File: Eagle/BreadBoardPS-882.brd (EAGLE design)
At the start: 36.5 x 16.5 mm, 6 parts

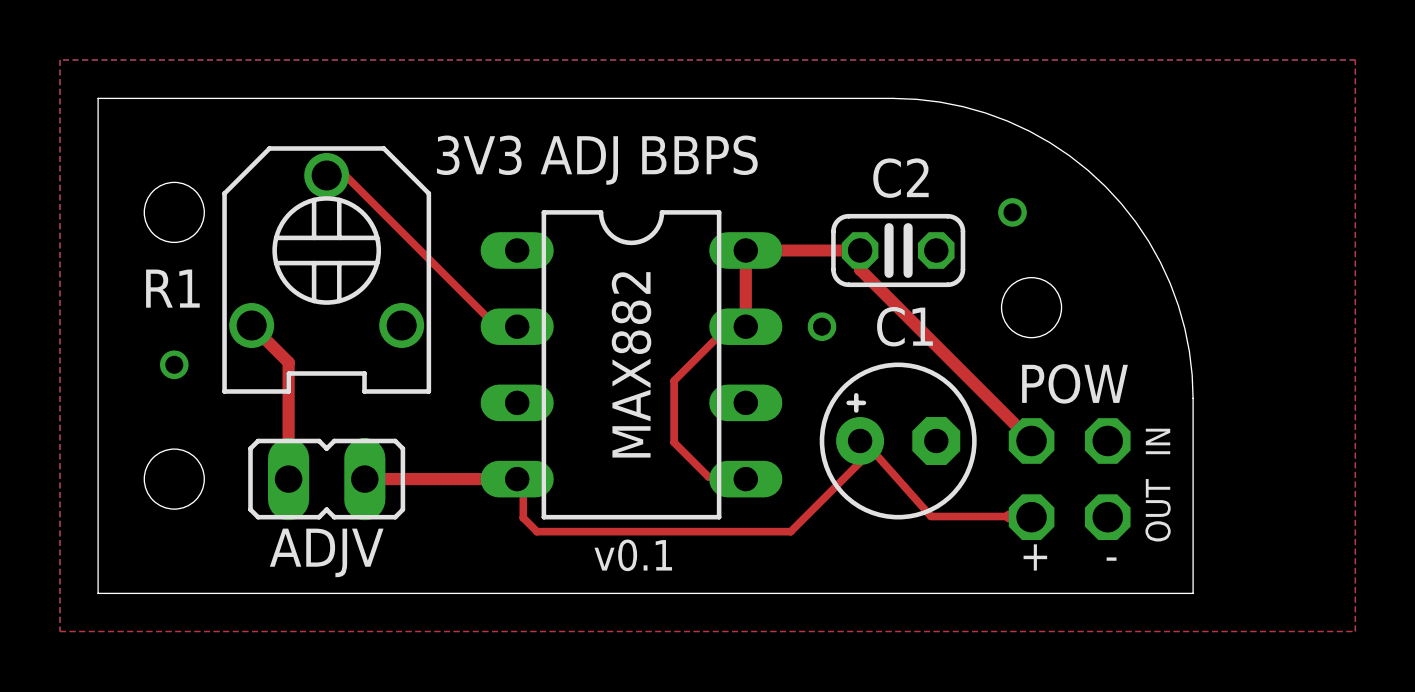
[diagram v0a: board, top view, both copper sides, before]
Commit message: Board 0.2. Fixed mount holes, power in/out, silk on bottom. New gerbers.
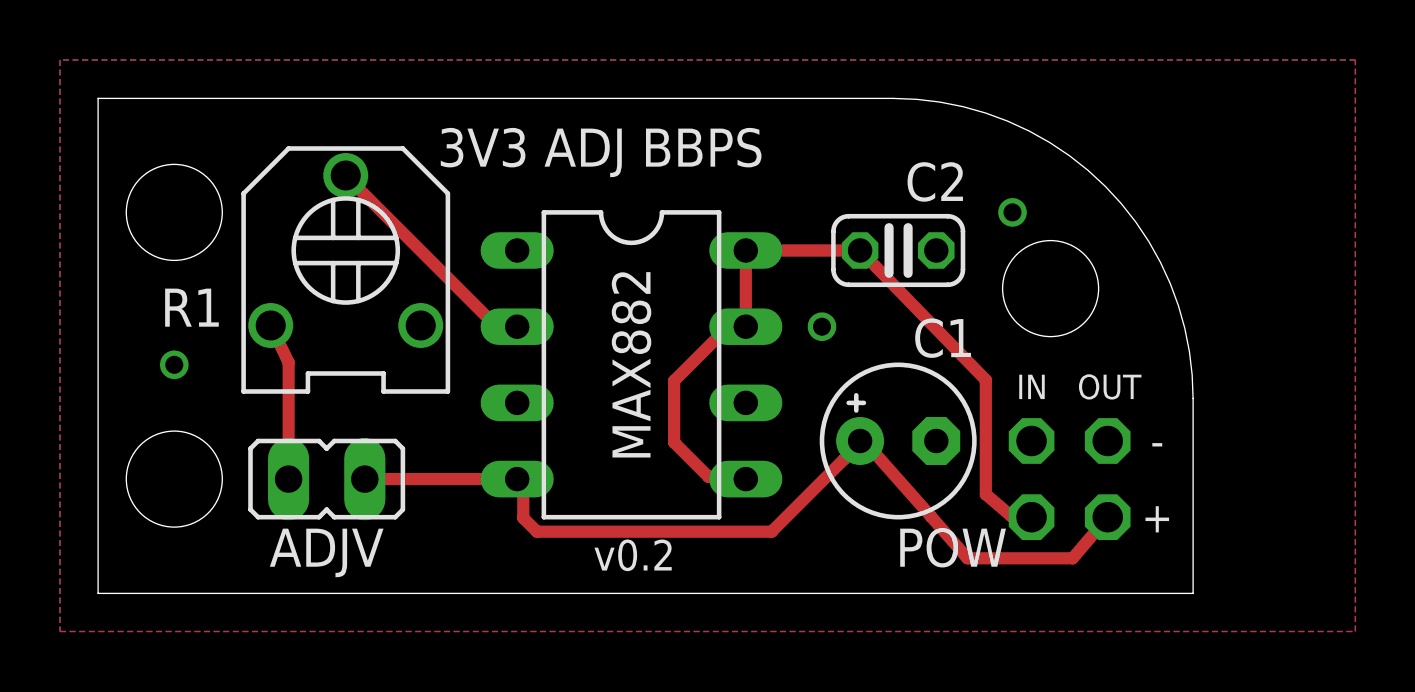
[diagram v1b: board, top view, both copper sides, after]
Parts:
- moved POW 7.18 mm to (37.5, 3.81), turned to 270 degrees
- moved R1 0.64 mm to (8.26, 11.4)
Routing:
- net N$4: track 26.7 -> 30.1 mm
- net N$1: track 23.6 -> 26.5 mm
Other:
- board text added: "v0.2"
- board text removed: "v0.1"
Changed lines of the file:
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@@
 <setting verticaltext="up"/>
 </settings>
-<grid distance="0.05" unitdist="inch" unit="inch" style="lines" multiple="1" display="yes" altdistance="0.025" altunitdist="inch" altunit="inch"/>
+<grid distance="0.05" unitdist="inch" unit="inch" style="lines" multiple="1" display="yes" altdistance="0.005" altunitdist="inch" altunit="inch"/>
 <layers>
 <layer number="1" name="Top" color="4" fill="1" visible="yes" active="yes"/>
@@
 <wire x1="26.5" y1="16.5" x2="0" y2="16.5" width="0" layer="20"/>
 <wire x1="0" y1="16.5" x2="0" y2="0" width="0" layer="20"/>
-<hole x="2.54" y="12.7" drill="2"/>
-<hole x="2.54" y="3.81" drill="2"/>
-<hole x="31.115" y="9.525" drill="2"/>
-<text x="11.176" y="13.97" size="1.27" layer="25">3V3 ADJ BBPS</text>
-<text x="34.925" y="5.588" size="0.8128" layer="25" rot="R270">IN</text>
-<text x="34.925" y="3.81" size="0.8128" layer="25" rot="R270">OUT</text>
-<text x="19.685" y="13.97" size="0.8128" layer="26" distance="40" rot="MR270">3V3, or close ADJV
+<hole x="2.54" y="12.7" drill="3.2"/>
+<hole x="2.54" y="3.81" drill="3.2"/>
+<hole x="31.75" y="10.16" drill="3.2"/>
+<text x="11.303" y="14.224" size="1.27" layer="25">3V3 ADJ BBPS</text>
+<text x="30.607" y="6.477" size="0.8128" layer="25">IN</text>
+<text x="32.639" y="6.477" size="0.8128" layer="25">OUT</text>
+<text x="19.431" y="14.478" size="0.8128" layer="26" distance="40" rot="MR270">3V3, or close ADJV
 for adj voltage.
 Max current: 200mA</text>
-<text x="31.242" y="1.778" size="1.016" layer="25" align="top-center">+</text>
-<text x="33.782" y="1.778" size="1.016" layer="25" align="top-center">-</text>
-<text x="16.51" y="0.762" size="1.016" layer="25">v0.1</text>
+<text x="35.306" y="3.048" size="1.016" layer="25" align="top-center">+</text>
+<text x="35.306" y="5.588" size="1.016" layer="25" align="top-center">-</text>
+<text x="16.51" y="0.762" size="1.016" layer="25">v0.2</text>
 </plain>
 <attributes>
@@
 <elements>
 <element name="C1" library="rcl" package="E2,5-5" value="1uF" x="26.67" y="5.08" smashed="yes">
-<attribute name="NAME" x="26.924" y="8.255" size="1.27" layer="25" ratio="10" align="bottom-center"/>
+<attribute name="NAME" x="28.194" y="7.874" size="1.27" layer="25" ratio="10" align="bottom-center"/>
 <attribute name="VALUE" x="29.083" y="2.667" size="1.27" layer="27" ratio="10"/>
 </element>
 <element name="C2" library="resistor" package="C025-024X044" value="0.1uF" x="26.67" y="11.43" smashed="yes">
-<attribute name="NAME" x="26.797" y="13.208" size="1.27" layer="25" ratio="10" align="bottom-center"/>
+<attribute name="NAME" x="27.94" y="13.081" size="1.27" layer="25" ratio="10" align="bottom-center"/>
 <attribute name="VALUE" x="24.892" y="8.763" size="1.27" layer="27" ratio="10"/>
 </element>
@@
 <attribute name="VALUE" x="13.97" y="12.7" size="1.27" layer="27"/>
 </element>
-<element name="R1" library="dp_devices" package="TRIMMER_3306F" value="10k" x="7.62" y="11.43" smashed="yes">
-<attribute name="NAME" x="2.4892" y="9.525" size="1.27" layer="25" ratio="10" align="bottom-center"/>
-<attribute name="VALUE" x="3.62" y="4.43" size="1.778" layer="27" ratio="10"/>
-</element>
-<element name="POW" library="pinhead" package="2X02/90" value="" x="32.385" y="-1.27" smashed="yes" rot="R180">
-<attribute name="NAME" x="32.512" y="6.35" size="1.27" layer="25" ratio="10" align="bottom-center"/>
-<attribute name="VALUE" x="27.94" y="2.54" size="1.27" layer="27" rot="R270"/>
+<element name="R1" library="dp_devices" package="TRIMMER_3306F" value="10k" x="8.255" y="11.43" smashed="yes">
+<attribute name="NAME" x="3.1242" y="8.89" size="1.27" layer="25" ratio="10" align="bottom-center"/>
+<attribute name="VALUE" x="4.255" y="4.43" size="1.778" layer="27" ratio="10"/>
+</element>
+<element name="POW" library="pinhead" package="2X02/90" value="" x="37.465" y="3.81" smashed="yes" rot="R270">
+<attribute name="NAME" x="28.448" y="2.159" size="1.27" layer="25" ratio="10" rot="R180" align="bottom-center"/>
+<attribute name="VALUE" x="33.655" y="-0.635" size="1.27" layer="27"/>
 </element>
 </elements>
@@
 <contactref element="MAX882" pad="5"/>
 <contactref element="MAX882" pad="8"/>
-<wire x1="20.3454" y1="3.8862" x2="21.4884" y2="3.8862" width="0.254" layer="1"/>
-<wire x1="19.2024" y1="5.0292" x2="20.3454" y2="3.8862" width="0.254" layer="1"/>
-<wire x1="19.2024" y1="7.0866" x2="19.2024" y2="5.0292" width="0.254" layer="1"/>
-<wire x1="20.8026" y1="8.6868" x2="19.2024" y2="7.0866" width="0.254" layer="1"/>
+<wire x1="20.3454" y1="3.8862" x2="21.4884" y2="3.8862" width="0.4064" layer="1"/>
+<wire x1="19.2024" y1="5.0292" x2="20.3454" y2="3.8862" width="0.4064" layer="1"/>
+<wire x1="19.2024" y1="7.0866" x2="19.2024" y2="5.0292" width="0.4064" layer="1"/>
+<wire x1="20.8026" y1="8.6868" x2="19.2024" y2="7.0866" width="0.4064" layer="1"/>
 <wire x1="21.4884" y1="3.8862" x2="21.59" y2="3.81" width="0.254" layer="1"/>
 <wire x1="24.9174" y1="11.43" x2="25.4" y2="11.43" width="0.254" layer="16"/>
@@
 <wire x1="21.59" y1="11.43" x2="25.4" y2="11.43" width="0.4064" layer="1"/>
 <contactref element="POW" pad="3"/>
-<wire x1="25.4" y1="11.43" x2="25.4" y2="10.795" width="0.4064" layer="1"/>
-<wire x1="25.4" y1="10.795" x2="31.115" y2="5.08" width="0.4064" layer="1"/>
+<wire x1="25.4" y1="11.43" x2="29.591" y2="7.112" width="0.4064" layer="1"/>
+<wire x1="29.591" y1="7.112" x2="29.591" y2="3.302" width="0.4064" layer="1"/>
+<wire x1="29.591" y1="3.302" x2="30.48" y2="2.54" width="0.4064" layer="1"/>
+<wire x1="30.48" y1="2.54" x2="31.115" y2="2.54" width="0.4064" layer="1"/>
 </signal>
 <signal name="N$4">
@@
 <contactref element="MAX882" pad="4"/>
 <contactref element="ADJV" pad="1"/>
-<wire x1="27.7622" y1="2.5654" x2="30.3784" y2="2.5654" width="0.254" layer="1"/>
-<wire x1="25.3746" y1="5.2578" x2="27.7622" y2="2.5654" width="0.254" layer="1"/>
+<wire x1="27.7622" y1="2.5654" x2="28.9814" y2="1.1684" width="0.4064" layer="1"/>
+<wire x1="25.3746" y1="5.2578" x2="27.7622" y2="2.5654" width="0.4064" layer="1"/>
 <wire x1="25.3746" y1="5.2578" x2="25.4" y2="5.08" width="0.254" layer="1"/>
-<wire x1="14.1732" y1="2.5146" x2="14.1732" y2="3.6576" width="0.254" layer="1"/>
-<wire x1="14.6304" y1="2.0574" x2="14.1732" y2="2.5146" width="0.254" layer="1"/>
-<wire x1="23.0886" y1="2.0574" x2="14.6304" y2="2.0574" width="0.254" layer="1"/>
-<wire x1="25.3746" y1="4.3434" x2="23.0886" y2="2.0574" width="0.254" layer="1"/>
-<wire x1="25.3746" y1="5.0292" x2="25.3746" y2="4.3434" width="0.254" layer="1"/>
+<wire x1="14.1732" y1="2.5146" x2="14.1732" y2="3.6576" width="0.4064" layer="1"/>
+<wire x1="14.6304" y1="2.0574" x2="14.1732" y2="2.5146" width="0.4064" layer="1"/>
+<wire x1="22.4536" y1="2.0574" x2="14.6304" y2="2.0574" width="0.4064" layer="1"/>
+<wire x1="24.8666" y1="4.4704" x2="22.4536" y2="2.0574" width="0.4064" layer="1"/>
+<wire x1="25.3746" y1="5.0292" x2="24.8666" y2="4.4704" width="0.4064" layer="1"/>
 <wire x1="14.1732" y1="3.6576" x2="13.97" y2="3.81" width="0.254" layer="1"/>
 <wire x1="25.3746" y1="5.0292" x2="25.4" y2="5.08" width="0.254" layer="1"/>
 <wire x1="13.97" y1="3.81" x2="8.89" y2="3.81" width="0.4064" layer="1"/>
 <contactref element="POW" pad="4"/>
-<wire x1="30.3784" y1="2.5654" x2="31.0896" y2="2.5654" width="0.4064" layer="1"/>
-<wire x1="31.0896" y1="2.5654" x2="31.115" y2="2.54" width="0.4064" layer="1"/>
+<wire x1="28.9814" y1="1.1684" x2="32.4866" y2="1.1684" width="0.4064" layer="1"/>
+<wire x1="32.4866" y1="1.1684" x2="33.655" y2="2.54" width="0.4064" layer="1"/>
 </signal>
 <signal name="N$3">
@@
 <contactref element="ADJV" pad="2"/>
 <wire x1="6.35" y1="3.81" x2="6.35" y2="7.7" width="0.4064" layer="1"/>
-<wire x1="6.35" y1="7.7" x2="5.12" y2="8.93" width="0.4064" layer="1"/>
+<wire x1="6.35" y1="7.7" x2="5.755" y2="8.93" width="0.4064" layer="1"/>
 </signal>
 <signal name="N$5">
 <contactref element="MAX882" pad="2"/>
 <contactref element="R1" pad="2"/>
-<wire x1="13.2588" y1="8.9154" x2="13.9446" y2="8.9154" width="0.254" layer="1"/>
-<wire x1="8.2296" y1="13.9446" x2="13.2588" y2="8.9154" width="0.254" layer="1"/>
+<wire x1="13.2588" y1="8.9154" x2="13.9446" y2="8.9154" width="0.4064" layer="1"/>
+<wire x1="8.2296" y1="13.9446" x2="13.2588" y2="8.9154" width="0.4064" layer="1"/>
 <wire x1="7.7724" y1="13.9446" x2="8.2296" y2="13.9446" width="0.254" layer="1"/>
 <wire x1="13.9446" y1="8.9154" x2="13.97" y2="8.89" width="0.254" layer="1"/>
-<wire x1="7.7724" y1="13.9446" x2="7.62" y2="13.93" width="0.254" layer="1"/>
+<wire x1="7.7724" y1="13.9446" x2="8.255" y2="13.93" width="0.4064" layer="1"/>
 </signal>
 <signal name="GND">

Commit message: Fixed C1 on schematic (and updated the board), README notes.
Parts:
- C1: value 1uF -> 2K2uF
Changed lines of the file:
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@@
 </autorouter>
 <elements>
-<element name="C1" library="rcl" package="E2,5-5" value="1uF" x="26.67" y="5.08" smashed="yes">
+<element name="C1" library="rcl" package="E2,5-5" value="2K2uF" x="26.67" y="5.08" smashed="yes">
 <attribute name="NAME" x="28.194" y="7.874" size="1.27" layer="25" ratio="10" align="bottom-center"/>
 <attribute name="VALUE" x="29.083" y="2.667" size="1.27" layer="27" ratio="10"/>

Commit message: Fixed the schematic again because I didn't fix it correctly the first time. My bad.
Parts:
- C1: value 2K2uF -> 2.2uF
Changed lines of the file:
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@@
 <?xml version="1.0" encoding="utf-8"?>
 <!DOCTYPE eagle SYSTEM "eagle.dtd">
-<eagle version="7.1.0">
+<eagle version="7.2.0">
 <drawing>
 <settings>
@@
 </autorouter>
 <elements>
-<element name="C1" library="rcl" package="E2,5-5" value="2K2uF" x="26.67" y="5.08" smashed="yes">
+<element name="C1" library="rcl" package="E2,5-5" value="2.2uF" x="26.67" y="5.08" smashed="yes">
 <attribute name="NAME" x="28.194" y="7.874" size="1.27" layer="25" ratio="10" align="bottom-center"/>
 <attribute name="VALUE" x="29.083" y="2.667" size="1.27" layer="27" ratio="10"/>
